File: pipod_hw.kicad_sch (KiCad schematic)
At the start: 4 parts, among them J1 SFV8R-2STE1HLF, J2 SFV14R-2STE1HLF, J7 USB_C_Receptacle_USB2.0

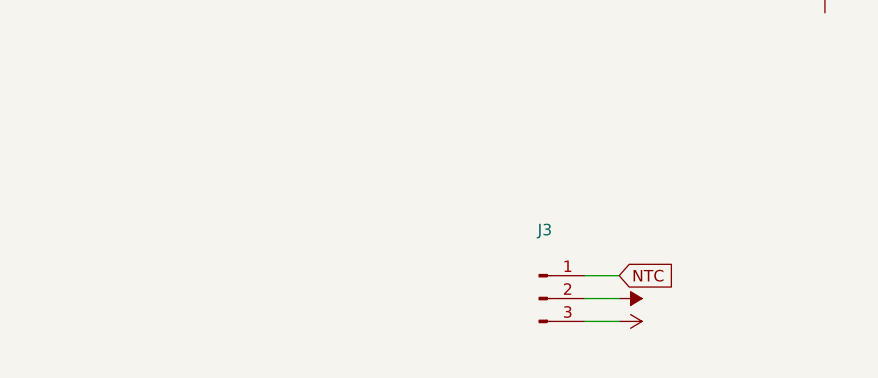
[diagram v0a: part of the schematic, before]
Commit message: schem: add LCSC lib, import DW01A
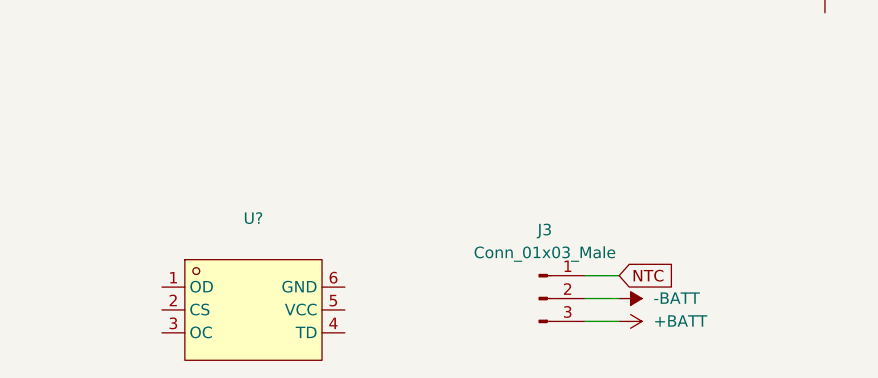
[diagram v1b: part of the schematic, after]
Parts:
- added U?: (no value), symbol lcsc:DW01A-G
- J3: value (none) -> Conn_01x03_Male; footprint (none) -> Gigahawk:Molex_PicoBlade_53047-0310_1x03_P1.25mm_Vertical
- J7: footprint (none) -> Gigahawk:USB_C_Receptacle_GCT_USB4085
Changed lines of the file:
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@@
     )
+  )
+  (symbol (lib_id "lcsc:DW01A-G") (at 138.43 124.46 0) (unit 1)
+    (in_bom yes) (on_board yes) (fields_autoplaced)
+    (property "Reference" "U?" (id 0) (at 138.43 114.3 0))
+    (property "Value" "" (id 1) (at 138.43 116.84 0))
+    (property "Footprint" "" (id 2) (at 138.43 134.62 0)
+      (effects (font (size 1.27 1.27)) hide)
+    )
+    (property "Datasheet" "https://lcsc.com/product-detail/Battery-Protection-ICs_DW01A-G_C61503.html" (id 3) (at 138.43 137.16 0)
+      (effects (font (size 1.27 1.27)) hide)
+    )
+    (property "Manufacturer" "FORTUNE" (id 4) (at 138.43 139.7 0)
+      (effects (font (size 1.27 1.27)) hide)
+    )
+    (property "LCSC Part" "C61503" (id 5) (at 138.43 142.24 0)
+      (effects (font (size 1.27 1.27)) hide)
+    )
+    (property "JLC Part" "Extended Part" (id 6) (at 138.43 144.78 0)
+      (effects (font (size 1.27 1.27)) hide)
+    )
+    (pin "1")
+    (pin "2")
+    (pin "3")
+    (pin "4")
+    (pin "5")
+    (pin "6")
   )
   (symbol (lib_id "power:-BATT") (at 179.07 123.19 270) (unit 1)
@@
       (effects (font (size 1.27 1.27)) hide)
     )
-    (property "Value" "" (id 1) (at 182.88 123.1899 90)
+    (property "Value" "-BATT" (id 1) (at 182.88 123.1899 90)
       (effects (font (size 1.27 1.27)) (justify left))
     )
@@
     (property "Reference" "J7" (id 0) (at 209.55 45.72 0))
     (property "Value" "USB_C_Receptacle_USB2.0" (id 1) (at 209.55 48.26 0))
-    (property "Footprint" "" (id 2) (at 213.36 68.58 0)
+    (property "Footprint" "Gigahawk:USB_C_Receptacle_GCT_USB4085" (id 2) (at 213.36 68.58 0)
       (effects (font (size 1.27 1.27)) hide)
     )
@@
     (in_bom yes) (on_board yes) (fields_autoplaced)
     (property "Reference" "J3" (id 0) (at 170.815 115.57 0))
-    (property "Value" "" (id 1) (at 170.815 118.11 0))
-    (property "Footprint" "" (id 2) (at 170.18 123.19 0)
+    (property "Value" "Conn_01x03_Male" (id 1) (at 170.815 118.11 0))
+    (property "Footprint" "Gigahawk:Molex_PicoBlade_53047-0310_1x03_P1.25mm_Vertical" (id 2) (at 170.18 123.19 0)
       (effects (font (size 1.27 1.27)) hide)
     )
@@
       (effects (font (size 1.27 1.27)) hide)
     )
-    (property "Value" "" (id 1) (at 182.88 125.7299 90)
+    (property "Value" "+BATT" (id 1) (at 182.88 125.7299 90)
       (effects (font (size 1.27 1.27)) (justify left))
     )
@@
       (reference "J7") (unit 1) (value "USB_C_Receptacle_USB2.0") (footprint "Gigahawk:USB_C_Receptacle_GCT_USB4085")
     )
-  )
+    (path "/16197c96-e9fd-4b9a-ac03-7dbecd60f449"
+      (reference "U?") (unit 1) (value "DW01A-G") (footprint "lcsc:SOT-23-6_L2.9-W1.6-P0.95-LS2.8-BR")
+    )
+  )

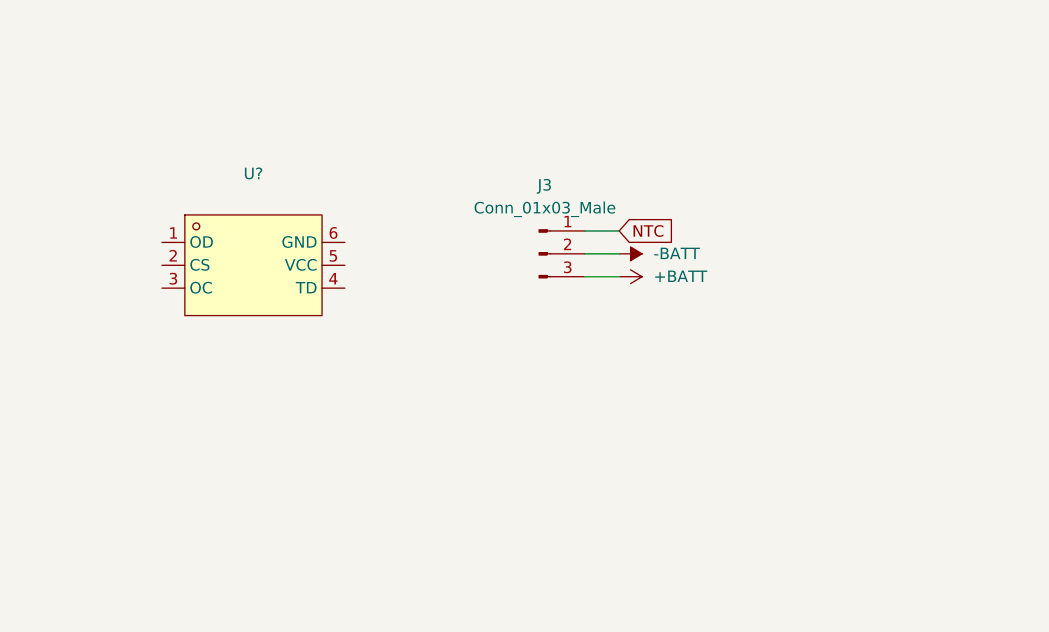
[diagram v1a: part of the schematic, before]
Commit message: schem: add battery protection
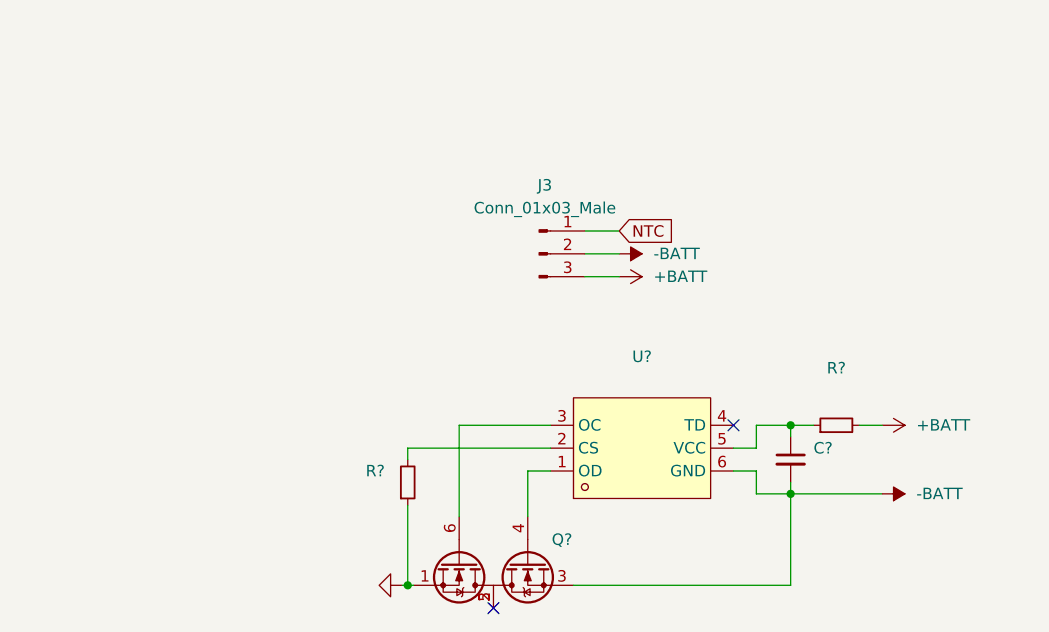
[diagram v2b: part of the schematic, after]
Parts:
- added C?: (no value), symbol Device:C_Small
- added Q?: (no value), lcsc:SOT-23-6_L2.9-W1.6-P0.95-LS2.8-BL, symbol lcsc:UMW8205A
- added R? (x2): (no value), symbol Device:R_Small
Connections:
- net +BATT: now also R?.2
- net -BATT: now also U?.6 (GND), C?.2, Q?.3 (S2)
- net at U?.1 (OD): now also Q?.4 (G2)
- net at U?.2 (CS): now also R?.2
- net at U?.3 (OC): now also Q?.6 (G1)
- net at U?.5 (VCC): now also C?.1, R?.1
- new net: Q?.2 (D1/D2), Q?.5 (D1/D2)
- new net GND: Q?.1 (S1), R?.1
- no-connect marks 0 -> 2
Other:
- moved on the sheet: U?

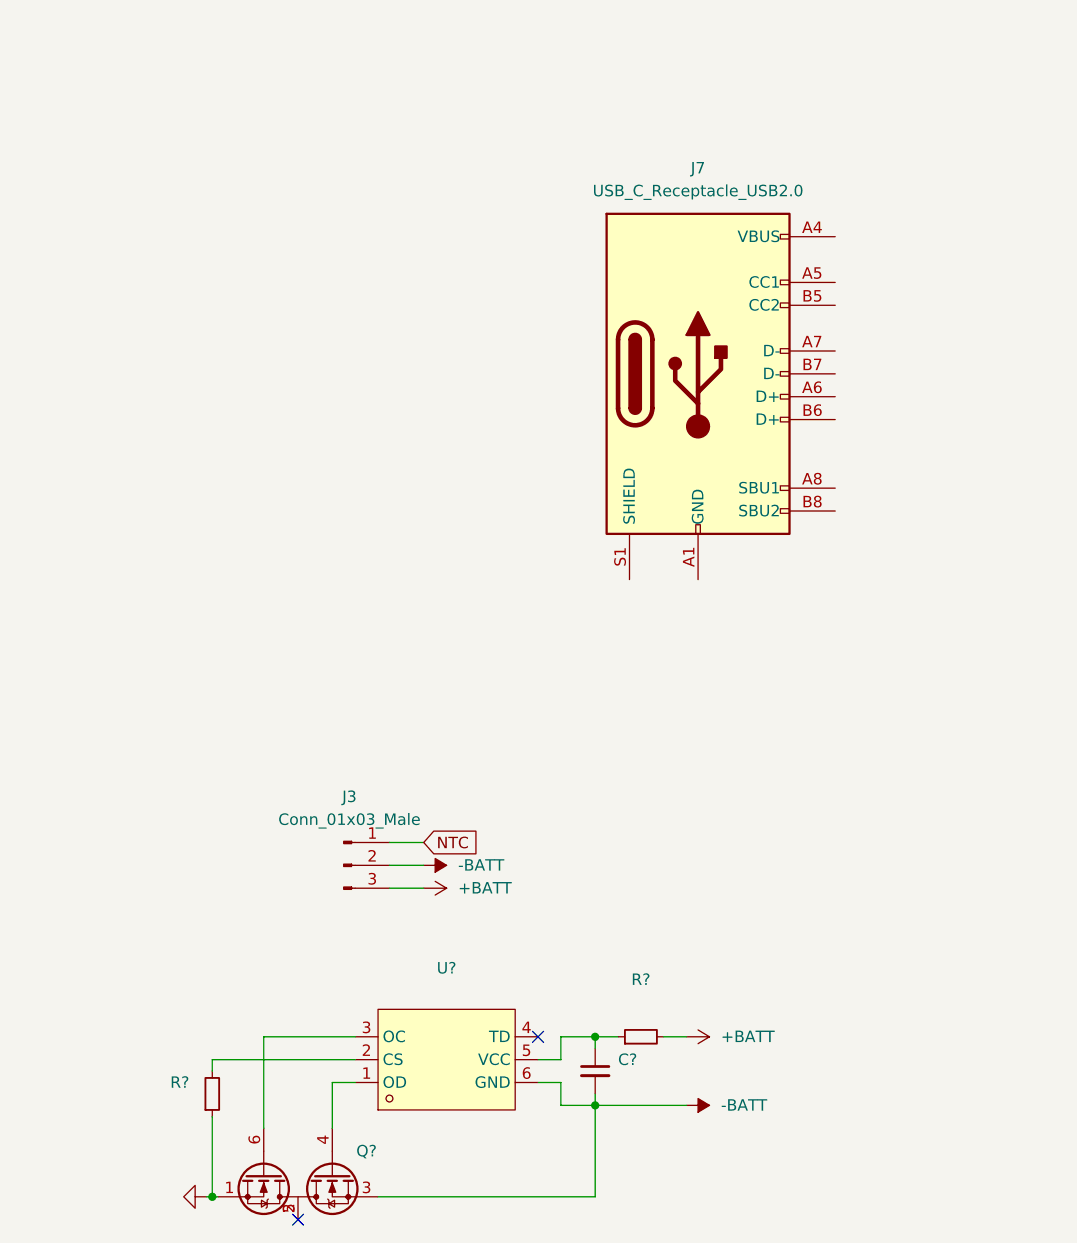
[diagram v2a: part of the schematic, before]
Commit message: schem: add battery charging, charger isolation
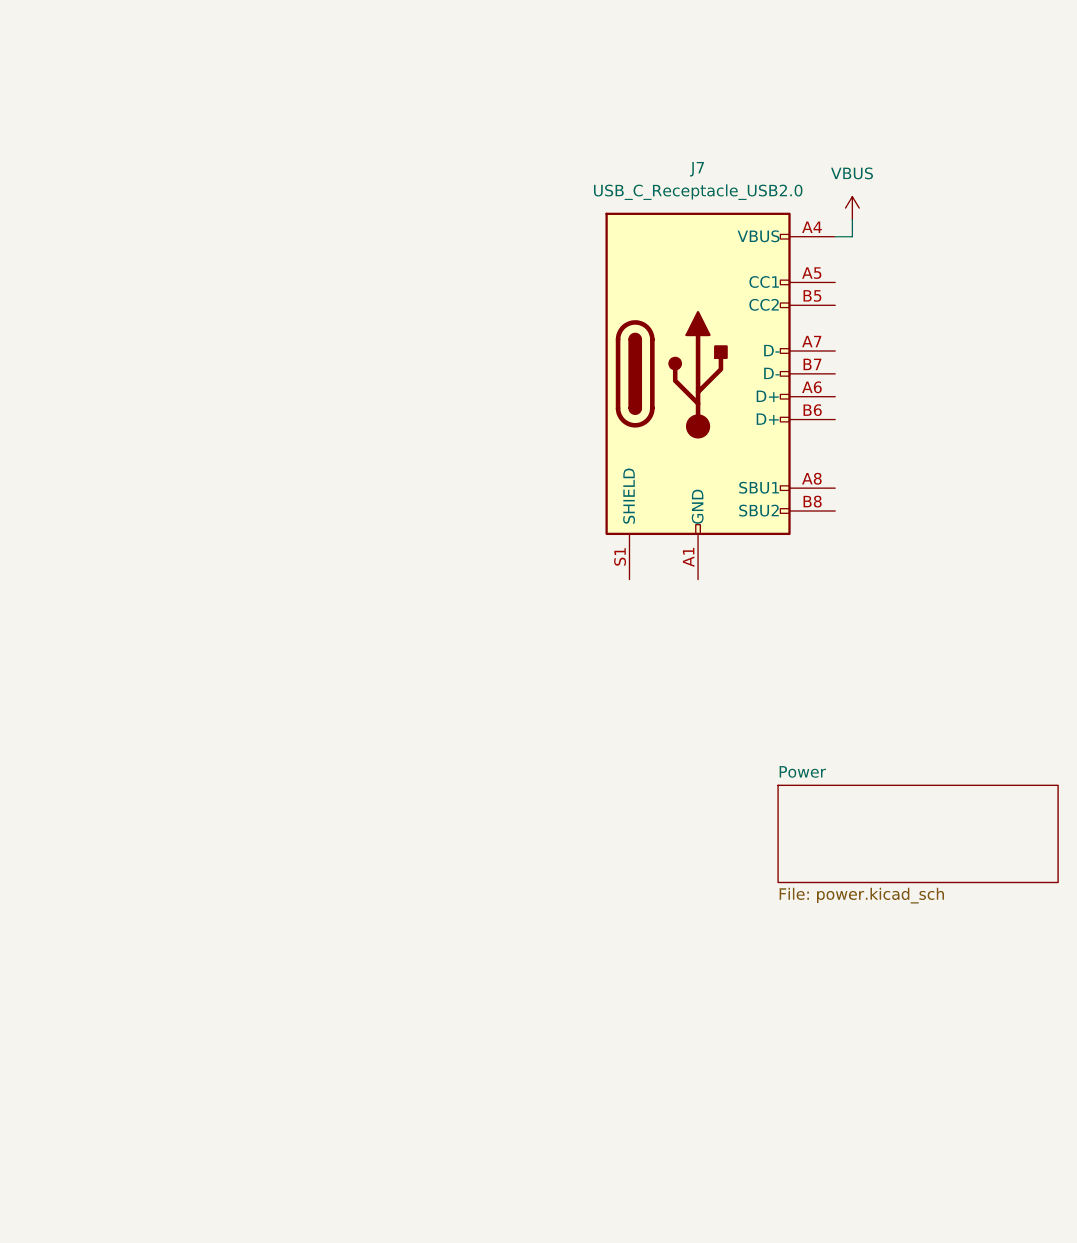
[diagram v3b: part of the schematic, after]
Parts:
- removed C?: (no value), symbol Device:C_Small
- removed J3: Conn_01x03_Male, Gigahawk:Molex_PicoBlade_53047-0310_1x03_P1.25mm_Vertical, symbol Connector:Conn_01x03_Male
- removed Q?: (no value), lcsc:SOT-23-6_L2.9-W1.6-P0.95-LS2.8-BL, symbol lcsc:UMW8205A
- removed R? (x2): (no value), symbol Device:R_Small
- removed U?: (no value), symbol lcsc:DW01A-G
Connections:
- net VBUS: now reaches J7.A4 (VBUS), J7.A9 (VBUS), J7.B4 (VBUS), J7.B9 (VBUS)
- no-connect marks 2 -> 0
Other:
- added sheet Power (power.kicad_sch)

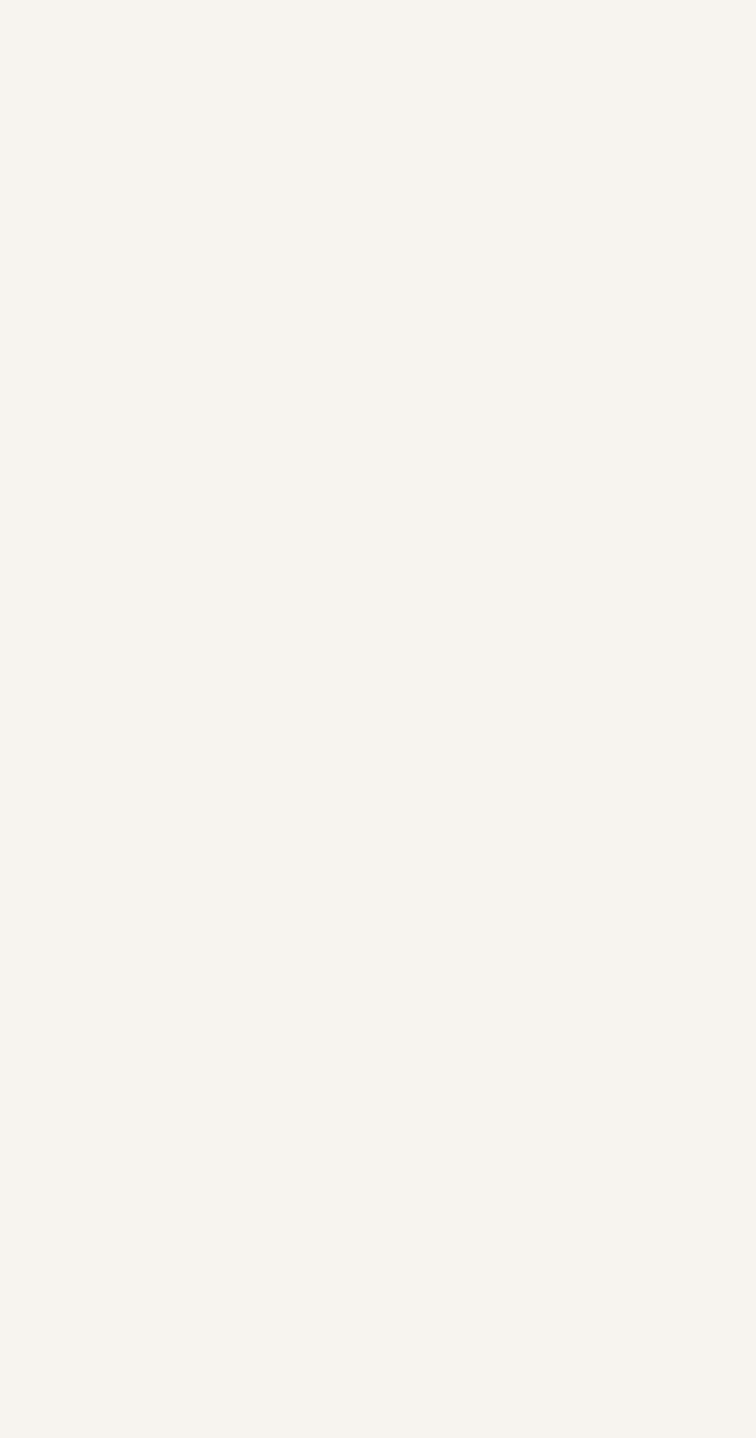
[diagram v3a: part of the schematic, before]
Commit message: schem: finish power design, start SMC design
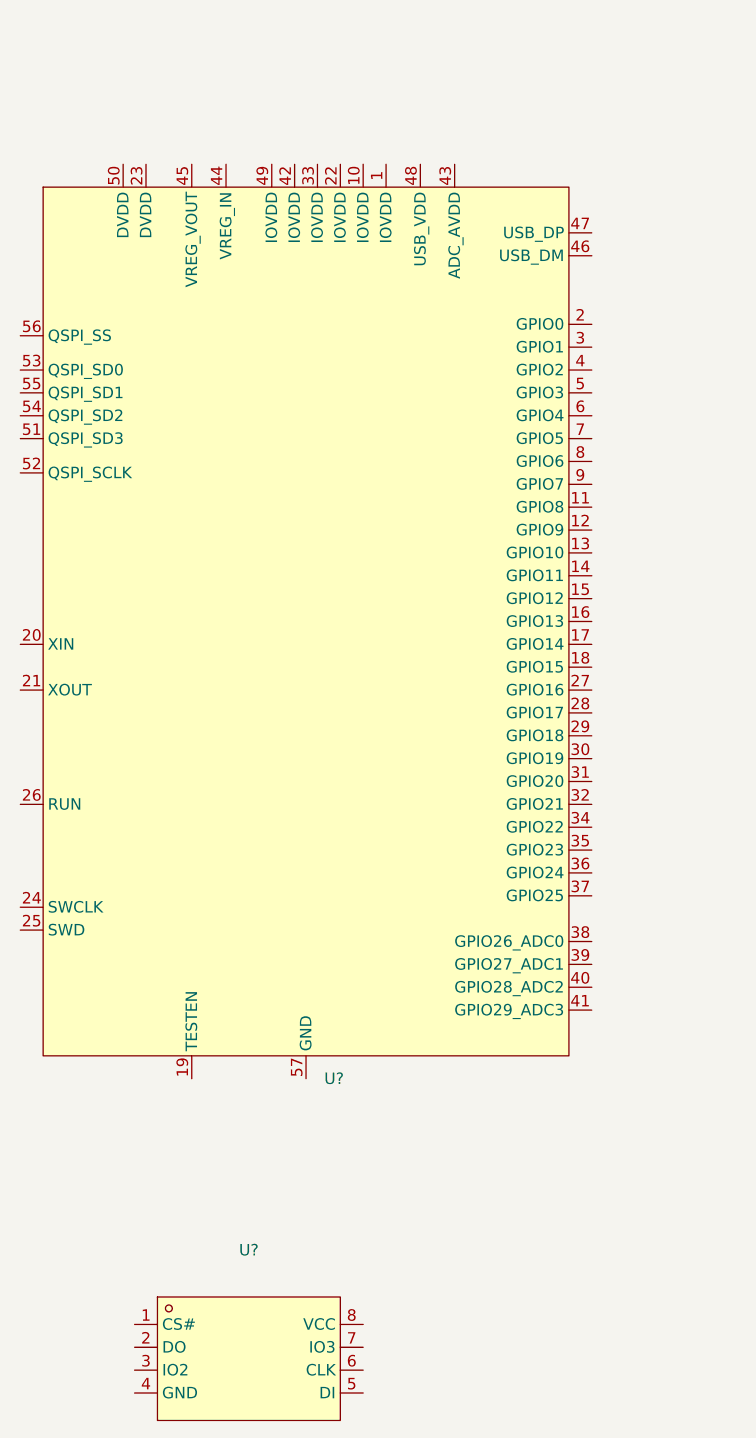
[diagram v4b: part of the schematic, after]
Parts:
- added U?: (no value), symbol lcsc:W25Q128JVSIQTR
- added U?: (no value), symbol lcsc:RP2040
